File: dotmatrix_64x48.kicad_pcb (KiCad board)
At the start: 2 copper layers, 226 x 136 mm, 720 parts, among them J1 CONN_01X04, J2 CONN_01X05, P3 CONN_01X06, P6 CONN_01X03, Q1 Q_NPN_BCE RN5006, Q10 AO3401, Q11 AO3401, Q12 AO3401, Q13 AO3401, Q14 AO3401, Q15 AO3401, Q16 AO3401, Q17 AO3401, Q18 AO3401, Q19 AO3401, Q2 Q_NPN_BEC, Q20 AO3401, Q21 AO3401, Q22 AO3401, Q23 AO3401, Q24 AO3401, Q25 AO3401, Q26 AO3401, Q27 AO3401, Q28 AO3401, Q29 AO3401, Q3 NJL7302L-F3, Q30 Q_NPN_BEC, Q4 Q_NPN_BEC, Q5 AO3401, Q6 AO3401, Q7 AO3401, Q8 AO3401, Q9 AO3401, SW1 SW_PUSH_SMALL_H, SW2 SW_PUSH_SMALL_H, SW3 SW_PUSH_SMALL_H, SW4 SW_PUSH_SMALL_H, SW5 SW_PUSH_SMALL_H, SW6 SW_PUSH_SMALL_H, SW7 SW_PUSH_SMALL_H, SW8 SW_PUSH_SMALL_H, T1 COMMON_MODE_CHOKE, U1 WROOM-02, U10 LED1642GW, U11 74HCT595, U12 AE-BME280, U13 74HCT595, U14 NJM2845DL1-33, U15 74HCT595, U17 OSRB38C9AA, U18 BME280, U19 PIC32MX220F032B-I/ML, U2 74VHC541, U3 LED1642GW, U4 LED1642GW, U5 LED1642GW, U6 LED1642GW, U7 LED1642GW, U8 LED1642GW, U9 LED1642GW, Y1 8MHz

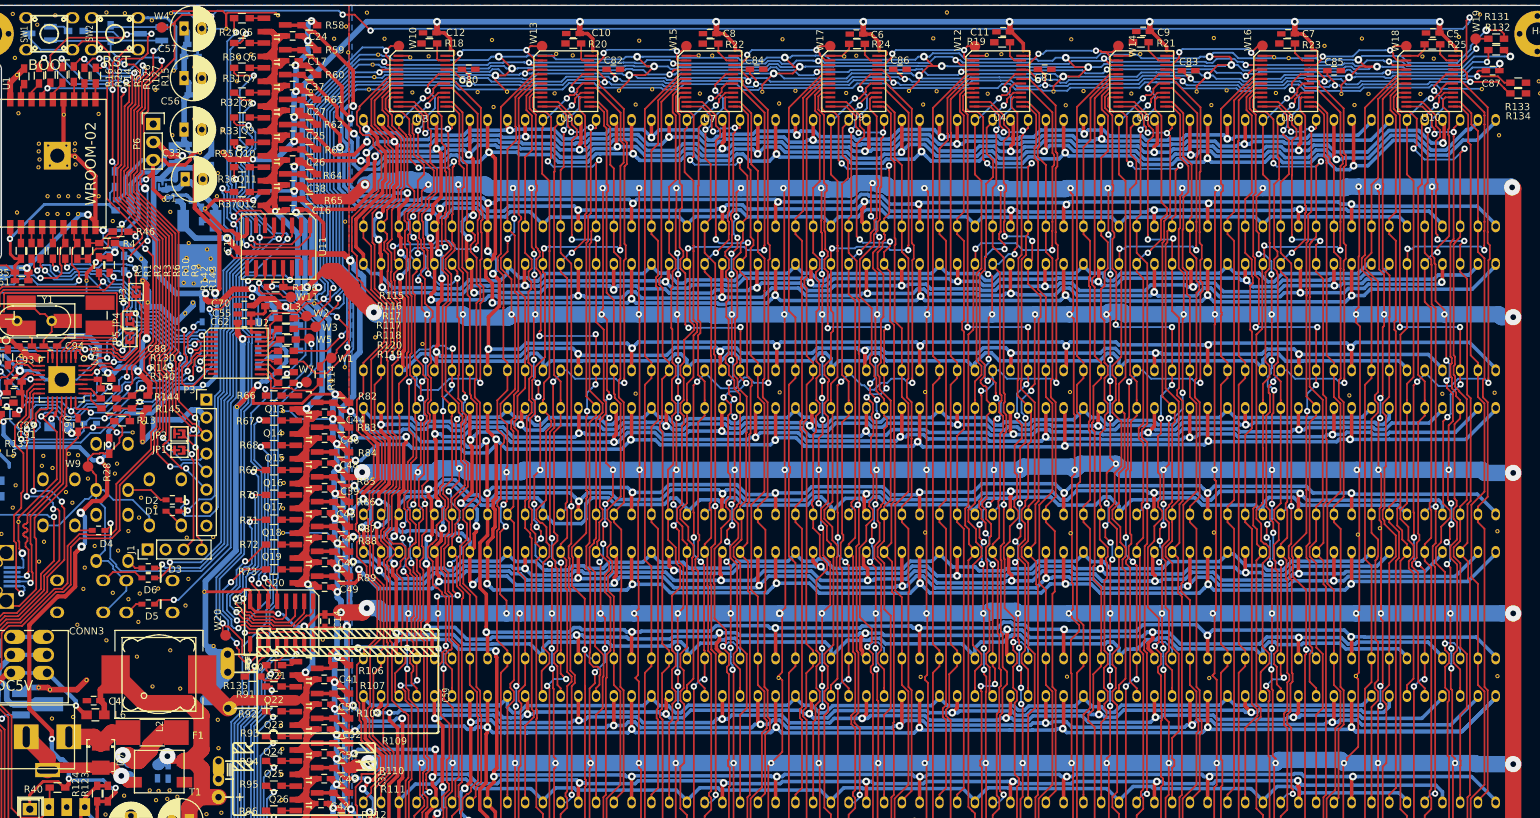
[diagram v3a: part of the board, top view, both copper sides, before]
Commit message: Improved GND impedance
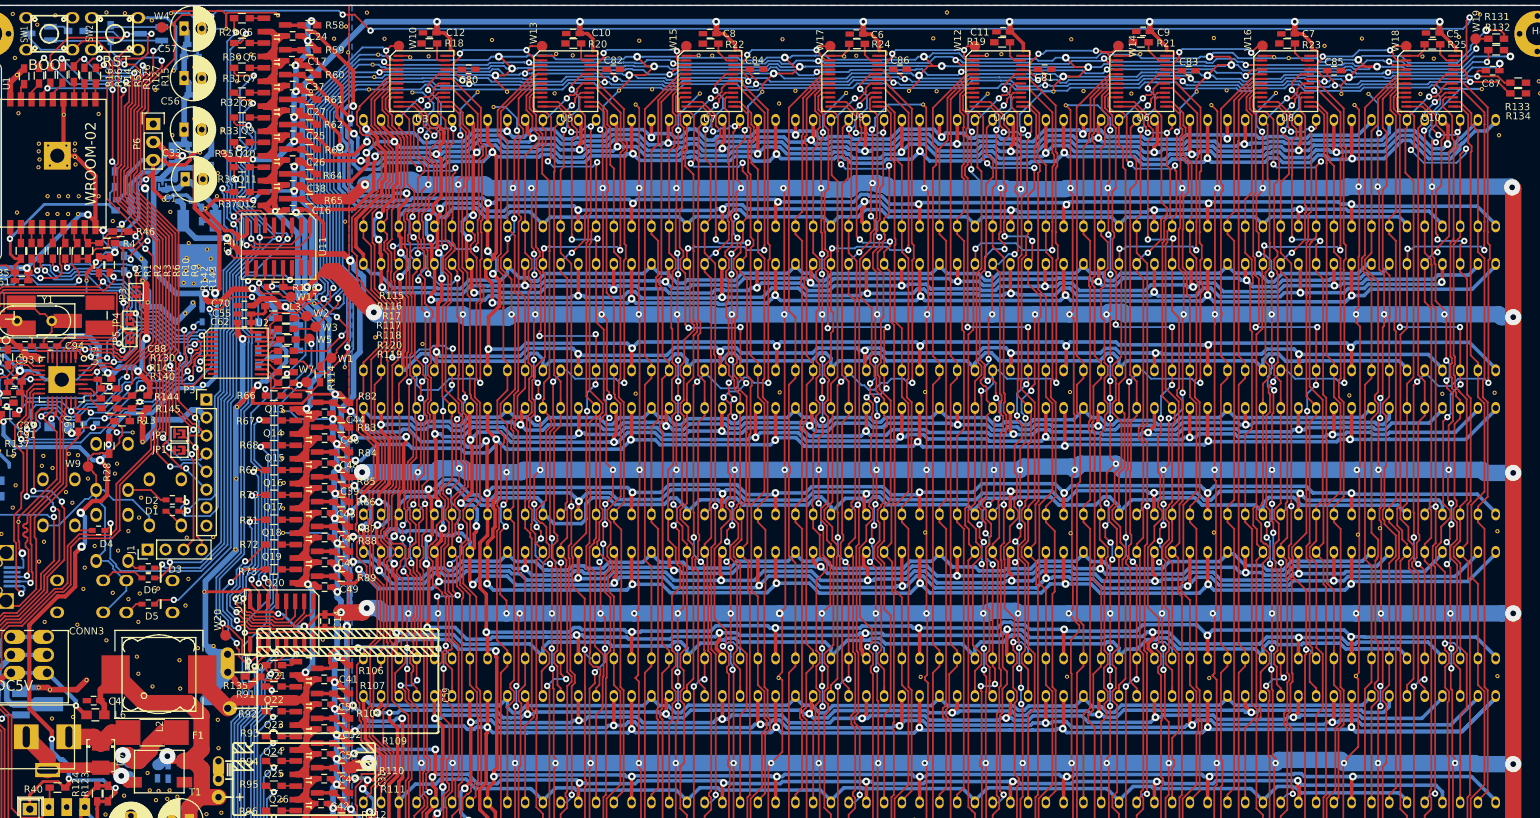
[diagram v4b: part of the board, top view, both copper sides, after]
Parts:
- added REF**: stitch-via-0.6mm, components:stitch-via-0.6mm, F.Cu at (50.6, 78.7)
- added REF**: stitch-via-0.6mm, components:stitch-via-0.6mm, F.Cu at (50.5, 88.7)
- added REF**: stitch-via-0.6mm, components:stitch-via-0.6mm, F.Cu at (23.6, 98.9)
- added REF**: stitch-via-0.6mm, components:stitch-via-0.6mm, F.Cu at (38.1, 120.2)
- added REF**: stitch-via-0.6mm, components:stitch-via-0.6mm, F.Cu at (45.2, 102.6)
- added REF**: stitch-via-0.6mm, components:stitch-via-0.6mm, F.Cu at (36.8, 106.2)
- moved REF** 1.91 mm to (42.6, 104.3)
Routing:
- net GND: track 5288.8 -> 5593.8 mm, vias 392 -> 409
- net r6: track 378.0 -> 381.5 mm
- net r4: track 364.4 -> 367.4 mm
- net r2: track 429.6 -> 426.9 mm
- net r7: track 416.7 -> 418.8 mm
- net ce5: track 114.7 -> 116.0 mm
- net co60: track 119.4 -> 120.8 mm
- net r5: track 408.9 -> 407.9 mm
- net ce28: track 94.3 -> 95.3 mm
- net ce21: track 113.8 -> 112.9 mm
- net ce54: track 105.8 -> 106.7 mm
- net ce53: track 114.0 -> 113.2 mm
- net ce55: track 107.6 -> 108.3 mm
- net co53: track 136.9 -> 137.6 mm
- net ce52: track 94.7 -> 94.2 mm
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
